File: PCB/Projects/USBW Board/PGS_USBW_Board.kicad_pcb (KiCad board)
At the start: 4 copper layers, 50.8 x 32.6 mm, 46 parts, among them IC1 BQ27621YZFR-G1A, J1 Molex 505110-1792, J2 USB4056-03-A, J4 PH 2.0 JST, P1 RPI-RM2, Q1 BSS138DW, Q2 BSS138DW, U1 USBLC6-2P6, U2 USBLC6-2P6, U3 USBLC6-2P6, U4 TPS63001DRCR, U5 BQ25180

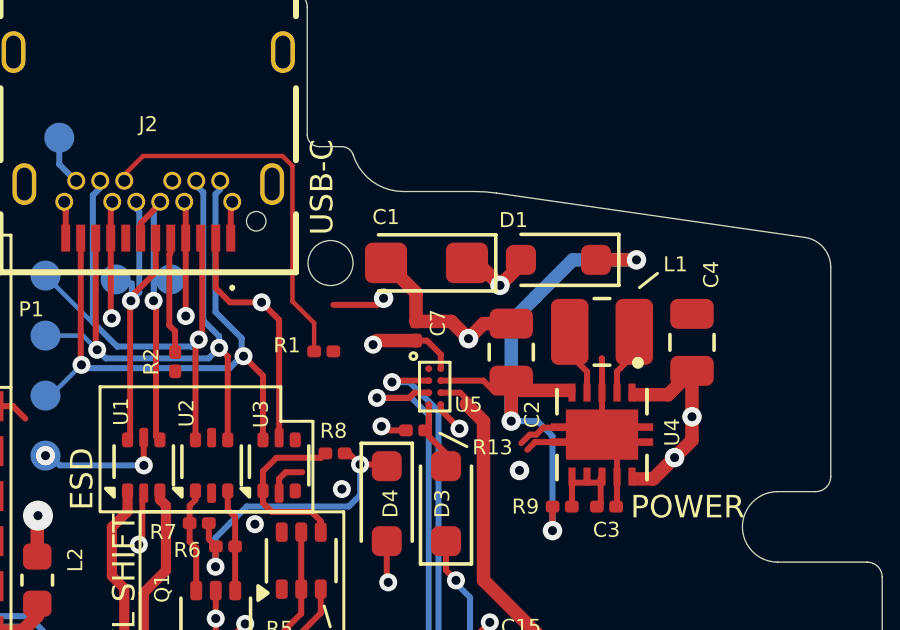
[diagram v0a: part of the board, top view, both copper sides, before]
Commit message: Sync local board work; replace Trigger Board with Trigger FPC
- Update Main, Stick and USBW board layouts, schematics and 3D exports
- Replace the rigid Trigger Board project with the new Trigger FPC design
- Add shared PCB/Libraries footprint library and fp-lib-table
- Regenerate production outputs (gerbers, drills, placement, BOM) for all boards
- Stop tracking KiCad auto-backup folders and fp-info-cache; consolidate .gitignore

Co-Authored-By: Claude Opus 5 <noreply@anthropic.com>
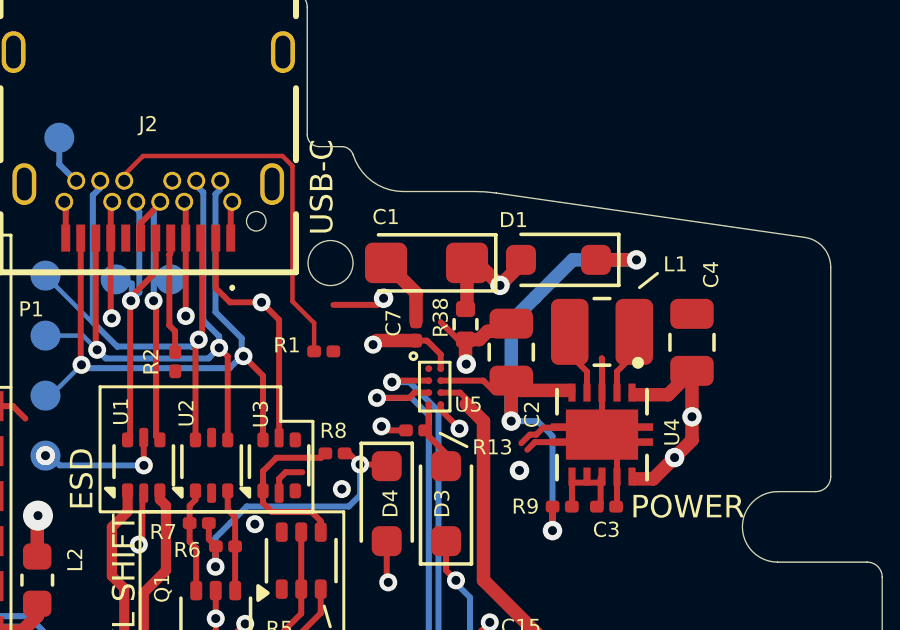
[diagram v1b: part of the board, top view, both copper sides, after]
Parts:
- added R38: 100k, Resistor_SMD:R_0402_1005Metric, F.Cu at (77.7, 28.6)
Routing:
- net +3.3V_PRE: track 30.0 -> 31.7 mm
- net GND: track 55.7 -> 56.4 mm
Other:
- board text added: "PGC USB+W Module"
- board text removed: "ProGCC 4 USB+W Module"

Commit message: Consolidate custom symbols, footprints and 3D models into repo library
Make the hardware repo self-contained instead of depending on the external
HHL-KiCad-Lib checkout and the missing progcc_v3 symbol library.

- New PCB/Libraries/ProGCC 4 Library.kicad_sym: the 12 custom symbols,
  extracted from the schematics' embedded caches (identical to what the
  boards use; duplicate hhl/progcc_v3 CUS08F30 merged)
- Library.pretty: add the 7 missing footprints and replace 9 that differed
  from the placed footprints with the hhl copies the boards match
- PCB/Libraries/3dmodels: STEP models previously referenced by absolute
  path into HHL-KiCad-Lib, now via ${KIPRJMOD}/../../Libraries/3dmodels
- Relink hhl:/progcc_v3:/RP2350_80QFN_minimal: references in all four
  schematics and PCBs to "ProGCC 4 Library"
- Project sym-lib-table and fp-lib-table for all four boards using
  ${KIPRJMOD}-relative paths (replaces Main's absolute fp-lib-table path)

No electrical change. ERC: lib_symbol_issues cleared (Main 70->49,
USBW 36->22, Stick 7->2, Trigger unchanged). DRC unchanged on all boards.

Co-Authored-By: Claude Opus 5.5 <noreply@anthropic.com>
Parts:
- IC1: footprint hhl:BGA9C50P3X3_162X158X62 -> ProGCC 4 Library:BGA9C50P3X3_162X158X62
- J1: footprint hhl:5051101792 -> ProGCC 4 Library:5051101792
- J2: footprint hhl:USB405603A -> ProGCC 4 Library:USB405603A
- P1: footprint hhl:RPI_RM2 -> ProGCC 4 Library:RPI_RM2
- U4: footprint hhl:VREG_V62_16624-01YE -> ProGCC 4 Library:VREG_V62_16624-01YE
- U5: footprint hhl:DSBGA -> ProGCC 4 Library:DSBGA
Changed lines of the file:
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@@
 		)
 	)
-	(footprint "hhl:DSBGA"
+	(footprint "ProGCC 4 Library:DSBGA"
 		(layer "F.Cu")
 		(at 76.625 30.725)
@@
 		)
 	)
-	(footprint "hhl:RPI_RM2"
+	(footprint "ProGCC 4 Library:RPI_RM2"
 		(layer "F.Cu")
 		(at 54.5 33.925)
@@
 		)
 		(embedded_fonts no)
-		(model "C:/Users/Mitch/GitRepos/HHL-KiCad-Lib/models/RM2MODULE.step"
+		(model "${KIPRJMOD}/../../Libraries/3dmodels/RM2MODULE.step"
 			(offset
 				(xyz 0 0 0)
@@
 		)
 	)
-	(footprint "hhl:BGA9C50P3X3_162X158X62"
+	(footprint "ProGCC 4 Library:BGA9C50P3X3_162X158X62"
 		(layer "F.Cu")
 		(at 78.6718 41.7656 90)
@@
 		)
 		(embedded_fonts no)
-		(model "C:/Users/Mitch/GitRepos/HHL-KiCad-Lib/models/BQ27621YZFR.stp"
+		(model "${KIPRJMOD}/../../Libraries/3dmodels/BQ27621YZFR.stp"
 			(offset
 				(xyz 0 0 0)
@@
 		)
 	)
-	(footprint "hhl:VREG_V62_16624-01YE"
+	(footprint "ProGCC 4 Library:VREG_V62_16624-01YE"
 		(layer "F.Cu")
 		(at 82.2 32.325 -90)
@@
 		)
 	)
-	(footprint "hhl:USB405603A"
+	(footprint "ProGCC 4 Library:USB405603A"
 		(layer "F.Cu")
 		(at 67.074998 19.573 180)
@@
 		)
 		(embedded_fonts no)
-		(model "C:/Users/Mitch/GitRepos/HHL-KiCad-Lib/models/USB4056-03-A.stp"
+		(model "${KIPRJMOD}/../../Libraries/3dmodels/USB4056-03-A.stp"
 			(offset
 				(xyz 0 0 0)
@@
 		)
 	)
-	(footprint "hhl:5051101792"
+	(footprint "ProGCC 4 Library:5051101792"
 		(layer "F.Cu")
 		(at 63.35 46.675)
@@
 		)
 		(embedded_fonts no)
-		(model "C:/Users/Mitch/GitRepos/HHL-KiCad-Lib/models/505110-1792.stp"
+		(model "${KIPRJMOD}/../../Libraries/3dmodels/505110-1792.stp"
 			(offset
 				(xyz 0 -1.450000026 0.01999999925)
